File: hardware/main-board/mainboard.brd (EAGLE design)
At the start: 160 x 100 mm, 51 parts, among them J2 ADDRESS BUS, J3 DATA BUS, J5 IO_ADDRESS, J6 IO_DATA, J7 IO_CONTROLS, U1 AS6C1008-55PCN, U2 CD4001BE, U4 SST39SF010A-70-4C-NHEMICROCHI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

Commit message: closer to layout complete for z80Computer
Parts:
- added LED10, LED11, LED12, LED13, LED14, LED15, LED16, LED17, LED18, LED19, LED20, LED21, LED22, LED23, LED24, LED25, LED26, LED27, LED28, LED29, LED30, LED31, LED8, LED9: (no value), leds:LED-1206
- added LED32: Read Enable, leds:LED-1206
- added LED33: Output Enable, leds:LED-1206
- added R19, R20: 100 R, passives:0805
- moved R9 252.2 mm to (115.6, 8.89), turned to 180 degrees
- moved R8 234.0 mm to (111.8, 35.6), turned to 90 degrees
- moved J1 233.8 mm to (123.2, 3.81), turned to 180 degrees
- moved R10 229.4 mm to (115.6, 95.2), turned to 180 degrees
- moved LED2 226.3 mm to (120.7, 7.62)
- moved C6 224.6 mm to (120.7, 62.2), turned to 270 degrees
- moved R1 222.0 mm to (114.3, 14.0), turned to 180 degrees
- moved LED1 218.2 mm to (119.4, 12.7)
- moved C4 215.1 mm to (114.3, 35.6), turned to 90 degrees
- moved U2 213.7 mm to (118.1, 48.3)
- moved LED5 213.5 mm to (119.4, 16.5)
- moved S3 210.9 mm to (123.2, 87.6), turned to 180 degrees
- moved C7 208.0 mm to (90.2, 41.9), turned to 90 degrees
- moved LED4 207.2 mm to (119.4, 20.3)
- moved U$2 201.9 mm to (120.7, 39.4), turned to 180 degrees
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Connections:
- new net N$19: LED32.A, R19.1
- new net N$21: LED33.A, R20.1
- new net READ_ENABLE_LOW#: R19.2, U$5.12
- new net WRITE_ENABLE_LOW#: R20.2, U$5.10
- net A0: now also LED8.A
- net A1: now also LED9.A
- net A10: now also LED18.A
- net A11: now also LED19.A
- net A12: now also LED20.A
- net A13: now also LED21.A
- net A14: now also LED22.A
- net A15: now also LED23.A
- net A2: now also LED10.A
- net A3: now also LED11.A
- net A4: now also LED12.A
- net A5: now also LED13.A
- net A6: now also LED14.A
- net A7: now also LED15.A
- net A8: now also LED16.A
- net A9: now also LED17.A
- net D0: now also LED24.A
- net D1: now also LED25.A
- net D2: now also LED26.A
- net D3: now also LED27.A
- net D4: now also LED28.A
- net D5: now also LED29.A
- net D6: now also LED30.A
- net D7: now also LED31.A
- net GND: now also LED10.C, LED11.C, LED12.C, LED13.C, LED14.C, LED15.C, LED16.C, LED17.C, LED18.C, LED19.C, LED20.C, LED21.C, LED22.C, LED23.C, LED24.C, LED25.C, LED26.C, LED27.C, LED28.C, LED29.C, LED30.C, LED31.C, LED32.C, LED33.C, LED8.C, LED9.C
- net READ_ENABLE_LOW: now also U$5.13
- net WRITE_ENABLE_LOW: now also U$5.11
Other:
- board size 160 x 100 mm -> 127 x 100 mm

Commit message: main board starting to route
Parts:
- moved S1 83.4 mm to (98.3, 5.08), turned to 90 degrees
- moved LED2 57.5 mm to (63.8, 15.9), turned to 270 degrees
- moved LED1 56.8 mm to (63.8, 24.0), turned to 90 degrees
- moved U1 54.7 mm to (8.64, 59.3), turned to 180 degrees
- moved C5 54.6 mm to (89.4, 36.7), turned to 180 degrees
- moved C7 54.6 mm to (41.1, 17.9), turned to 180 degrees
- moved LED5 50.2 mm to (87.5, 55.2), turned to 90 degrees
- moved R9 49.6 mm to (66.7, 17.3), turned to 0 degrees
- moved R10 49.2 mm to (122.4, 46.5), turned to 0 degrees
- moved C6 48.5 mm to (72.8, 54.4), turned to 180 degrees
- moved R1 48.4 mm to (66.7, 22.6), turned to 0 degrees
- moved R17 46.5 mm to (77.3, 40.3)
- moved R18 46.5 mm to (77.3, 42.8)
- moved U2 45.4 mm to (74.7, 35.2)
- moved LED7 44.4 mm to (81.7, 42.8)
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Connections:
- removed net A14: J2.16, LED22.A
- removed net A15: J2.17, LED23.A
- removed net N$20: IC1.20
- net A14-SWITCH: now also J2.16, LED22.A
- net A15-SRAM-A14: now also J2.17, LED23.A
- net IORQ: now also IC1.20
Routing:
- net V5: track 0.00 -> 558.5 mm
- net A11: track 0.00 -> 92.6 mm
- net A12: track 0.00 -> 88.5 mm
- net A13: track 0.00 -> 87.3 mm
- net A10: track 0.00 -> 87.1 mm
- net A14-SWITCH: track 0.00 -> 85.1 mm
- net A9: track 0.00 -> 82.5 mm
- net A15-SRAM-A14: track 0.00 -> 82.3 mm
- net A8: track 0.00 -> 78.9 mm
- net A7: track 0.00 -> 75.5 mm
- net A6: track 0.00 -> 71.8 mm
- net A5: track 0.00 -> 69.1 mm
- net A4: track 0.00 -> 66.7 mm
- net A3: track 0.00 -> 64.1 mm
- net A2: track 0.00 -> 62.7 mm
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
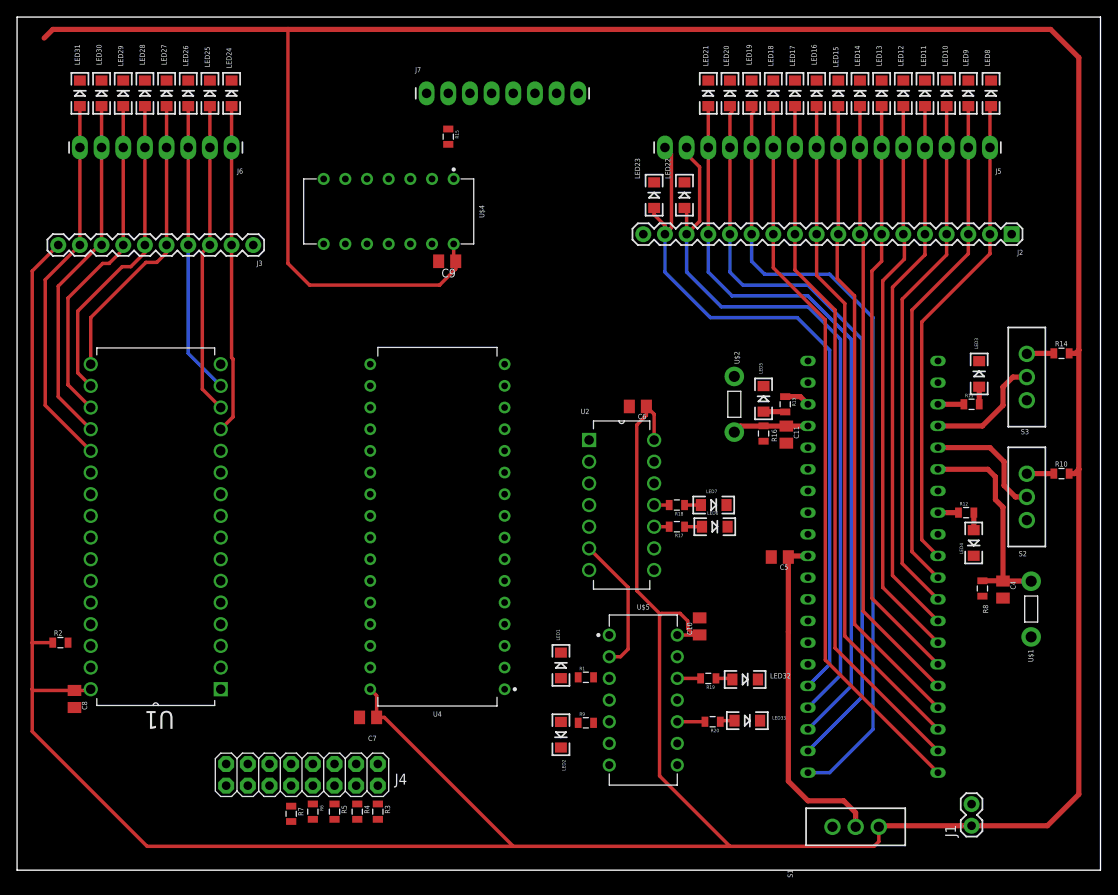
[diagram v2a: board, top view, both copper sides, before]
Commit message: update on clock board, so much cleaner now re-layout of main board
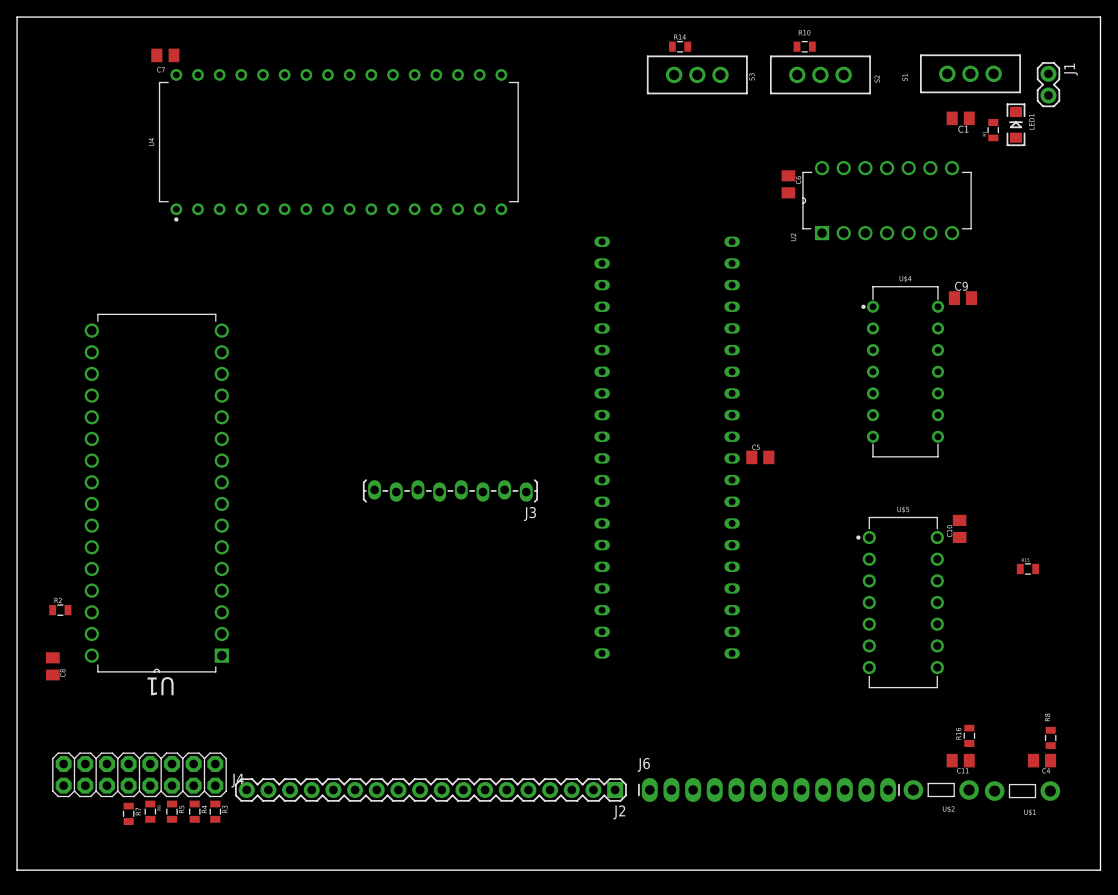
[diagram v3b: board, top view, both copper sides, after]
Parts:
- removed J5: IO_ADDRESS, connector:1X16_LONGPADS
- removed J7: IO_CONTROLS, connector:1X08_LONGPADS
- removed LED10, LED11, LED12, LED13, LED14, LED15, LED16, LED17, LED18, LED19, LED20, LED21, LED22, LED23, LED24, LED25, LED26, LED27, LED28, LED29, LED3, LED30, LED31, LED4, LED5, LED8, LED9: (no value), leds:LED-1206
- removed LED2: SRAM, leds:LED-1206
- removed LED32: Read Enable, leds:LED-1206
- removed LED33: Output Enable, leds:LED-1206
- removed LED6, LED7: OP Code Fetch, leds:LED-1206
- removed R11, R12, R13, R17, R18, R19, R20, R9: 100 R, passives:0805
- added C1: 10 uF, passives:C0805K
- J2: value ADDRESS BUS -> (none)
- J3: value DATA BUS -> (none); device connector:1X10 -> connector:1X08_LOCK_LONGPADS
- J6: value IO_DATA -> IO_CONTROLS; device connector:1X08_LONGPADS -> connector:1X12_LONGPADS
- LED1: value FLASH MEM -> (none)
- R1: value 100 R -> 1 K
- moved J6 89.9 mm to (74.2, 9.40), turned to 0 degrees
- moved S1 89.3 mm to (111.8, 93.3)
- moved J1 88.6 mm to (120.9, 93.3), turned to 270 degrees
- moved R15 84.8 mm to (118.5, 35.3), turned to 0 degrees
- moved LED1 82.8 mm to (117.1, 87.4)
- moved C7 81.1 mm to (17.4, 95.5)
- moved J2 80.0 mm to (70.1, 9.40)
- moved R1 80.0 mm to (114.4, 86.7), turned to 90 degrees
- moved U$4 63.4 mm to (104.1, 58.4), turned to 0 degrees
- moved C9 60.6 mm to (110.9, 67.1), turned to 0 degrees
- moved U2 58.6 mm to (109.6, 82.3), turned to 90 degrees
- moved R10 58.4 mm to (92.3, 96.5)
- moved R14 57.4 mm to (77.7, 96.5)
- moved S2 55.1 mm to (94.2, 93.2), turned to 270 degrees
- moved S3 52.4 mm to (79.7, 93.2), turned to 270 degrees
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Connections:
- removed net IRQ_ACK: R18.2, U2.11
- removed net N$10: LED3.A, R11.2
- removed net N$11: LED4.A, R12.2
- removed net N$12: IC1.28, R12.1
- removed net N$13: LED2.A, R9.1
- removed net N$14: IC1.18, R13.1
- removed net N$15: LED5.A, R13.2
- removed net N$17: LED6.A, R17.1
- removed net N$18: LED7.A, R18.1
- removed net N$19: LED32.A, R19.1
- removed net N$21: LED33.A, R20.1
- removed net N$3: C5.1, IC1.11, S1.2
- removed net OP_CODE_FETCH: R17.2, U2.10
- removed net READ_ENABLE_LOW#: R19.2, U$5.12
- removed net WRITE_ENABLE_LOW#: R20.2, U$5.10
- new net HALT: IC1.18, J6.11
- new net RFSH: IC1.28, J6.10
- new net VIN: J1.1, S1.3
- net A0: no longer J5.1, LED8.A
- net A1: no longer J5.2, LED9.A
- net A10: no longer J5.11, LED18.A
- net A11: no longer J5.12, LED19.A
- net A12: no longer J5.13, LED20.A
- net A13: no longer J5.14, LED21.A
- net A14-SWITCH: no longer J5.15, LED22.A
- net A15-SRAM-A14: no longer J5.16, LED23.A
- net A2: no longer J5.3, LED10.A
- net A3: no longer J5.4, LED11.A
- net A4: no longer J5.5, LED12.A
- net A5: no longer J5.6, LED13.A
- net A6: no longer J5.7, LED14.A
- net A7: no longer J5.8, LED15.A
- net A8: no longer J5.9, LED16.A
- net A9: no longer J5.10, LED17.A
- net BUSAK: now also J6.6; no longer J7.6, R11.1
- net BUSRQ: now also J6.7; no longer J7.7
- net D0: now also J3.1; no longer J3.2, J6.1, LED24.A
- net D1: now also J3.2; no longer J3.3, J6.2, LED25.A
- net D2: now also J3.3; no longer J3.4, J6.3, LED26.A
- net D3: now also J3.4; no longer J3.5, J6.4, LED27.A
- net D4: now also J3.5; no longer J3.6, J6.5, LED28.A
- net D5: now also J3.6; no longer J3.7, J6.6, LED29.A
- net D6: now also J3.7; no longer J3.8, J6.7, LED30.A
- net D7: now also J3.8; no longer J3.9, J6.8, LED31.A
- net FLASH_MEM_CS: no longer R1.2
- net GND: now also C1.2, J6.1; no longer J3.1, J7.1, LED10.C, LED11.C, LED12.C, LED13.C, LED14.C, LED15.C, LED16.C, LED17.C, LED18.C, LED19.C, LED2.C, LED20.C, LED21.C, LED22.C, LED23.C, LED24.C, LED25.C, LED26.C, LED27.C, LED28.C, LED29.C, LED3.C, LED30.C, LED31.C, LED32.C, LED33.C, LED4.C, LED5.C, LED6.C, LED7.C, LED8.C, LED9.C
- net INT: now also J6.2; no longer J7.2
- net IORQ: now also J6.8; no longer U2.13
- net M1: now also J6.9; no longer U2.12, U2.9
- net MREQ: no longer U2.8
- net READ_ENABLE_LOW: now also J6.4; no longer J7.4, U$5.13
- net SRAM_CS: no longer R9.2
- net SYS_CLK: now also J6.5; no longer J7.5
- net V5: now also C1.1, C5.1, IC1.11, J6.12, R1.2, S1.2; no longer J1.1, J3.10, J7.8, S1.3
- net WAIT: now also J6.3; no longer J7.3
- net WRITE_ENABLE_LOW: no longer U$5.11
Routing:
- net V5: track 558.5 -> 0.00 mm
- net A11: track 92.6 -> 0.00 mm
- net A12: track 88.5 -> 0.00 mm
- net A13: track 87.3 -> 0.00 mm
- net A10: track 87.1 -> 0.00 mm
- net A14-SWITCH: track 85.1 -> 0.00 mm
- net A9: track 82.5 -> 0.00 mm
- net A15-SRAM-A14: track 82.3 -> 0.00 mm
- net A8: track 78.9 -> 0.00 mm
- net A7: track 75.5 -> 0.00 mm
- net A6: track 71.8 -> 0.00 mm
- net A5: track 69.1 -> 0.00 mm
- net A4: track 66.7 -> 0.00 mm
- net A3: track 64.1 -> 0.00 mm
- net A2: track 62.7 -> 0.00 mm
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
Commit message: some routing complete
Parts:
- moved C6 33.5 mm to (123.2, 73.7), flipped to the bottom, turned to 90 degrees
- moved J3 23.7 mm to (50.7, 66.4)
- moved U2 11.3 mm to (103.8, 72.6), turned to 270 degrees
- moved C1 8.90 mm to (110.1, 97.0), flipped to the bottom, turned to 0 degrees
- moved R15 8.02 mm to (120.0, 43.2), flipped to the bottom, turned to 180 degrees
- moved C8 2.16 mm to (6.35, 23.9), flipped to the bottom
- moved C10 0.40 mm to (110.6, 40.4), flipped to the bottom
- moved R10 0.40 mm to (92.2, 96.9), flipped to the bottom, turned to 180 degrees
- moved C4 0.38 mm to (120.1, 12.4), flipped to the bottom, turned to 0 degrees
- moved R14 0.28 mm to (78.0, 96.6), flipped to the bottom, turned to 180 degrees
- moved R2 0.25 mm to (5.08, 30.2), flipped to the bottom, turned to 180 degrees
- moved R7 0.25 mm to (13.1, 6.86), flipped to the bottom
- moved C9 0.18 mm to (110.7, 67.2), flipped to the bottom, turned to 90 degrees
- moved C5 0.18 mm to (87.2, 48.3), flipped to the bottom, turned to 180 degrees
- moved C11 0.13 mm to (110.6, 12.7), flipped to the bottom, turned to 0 degrees
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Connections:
- net BUSAK: now also J6.4; no longer J6.6
- net IORQ: now also J6.10; no longer J6.8
- net M1: now also J6.8; no longer J6.9
- net READ_ENABLE_LOW: now also J6.3; no longer J6.4
- net RFSH: now also J6.9; no longer J6.10
- net SRAM-A15: now also J4.9; no longer J4.7
- net SRAM-A16: now also J4.7; no longer J4.9
- net WAIT: now also J6.6; no longer J6.3
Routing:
- net V5: track 0.00 -> 595.4 mm
- net A14-SWITCH: track 0.00 -> 126.2 mm
- net A12: track 0.00 -> 118.2 mm
- net A13: track 0.00 -> 107.9 mm
- net A11: track 0.00 -> 93.9 mm
- net A10: track 0.00 -> 75.2 mm
- net A9: track 0.00 -> 71.6 mm
- net A8: track 0.00 -> 68.0 mm
- net A7: track 0.00 -> 64.4 mm
- net A6: track 0.00 -> 60.8 mm
- net A5: track 0.00 -> 58.0 mm
- net RFSH: track 0.00 -> 54.2 mm
- net A4: track 0.00 -> 53.7 mm
- net A3: track 0.00 -> 50.1 mm
- net M1: track 0.00 -> 49.9 mm
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
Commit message: not sure
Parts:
- added U$3: CMD_C0DE_LOGOCMD_CODE_LOGO_SILK, logos:CMD_C0DE_LOGO_SILK
- J2: value (none) -> IO_ADDRESS
- J3: value (none) -> IO_DATA
- LED1: value (none) -> pwr
- S1: value (none) -> MAIN PWR
- moved R15 52.5 mm to (68.1, 35.6), turned to 0 degrees
- moved C5 20.2 mm to (67.1, 48.3), turned to 0 degrees
- moved IC1 2.54 mm to (78.7, 49.5), flipped to the top
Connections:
- net GND: now also J2.18; no longer J2.1
- net V5: now also J2.1; no longer J2.18
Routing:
- net WRITE_ENABLE_LOW: track 0.00 -> 186.4 mm, vias 0 -> 3
- net READ_ENABLE_LOW: track 21.6 -> 171.5 mm, vias 0 -> 3
- net D7: track 0.00 -> 146.5 mm, vias 0 -> 2
- net A7: track 64.4 -> 195.9 mm, vias 0 -> 3
- net A9: track 71.6 -> 198.2 mm, vias 0 -> 3
- net A8: track 68.0 -> 189.4 mm, vias 0 -> 2
- net D6: track 0.00 -> 119.2 mm, vias 0 -> 2
- net D4: track 0.00 -> 118.8 mm, vias 0 -> 3
- net D5: track 0.00 -> 116.9 mm, vias 0 -> 3
- net A4: track 53.7 -> 168.6 mm, vias 0 -> 4
- net A2: track 46.5 -> 160.7 mm, vias 0 -> 3
- net A10: track 75.2 -> 187.0 mm, vias 0 -> 2
- net A0: track 42.4 -> 154.2 mm, vias 0 -> 4
- net A3: track 50.1 -> 159.2 mm, vias 0 -> 3
- net A1: track 44.4 -> 153.2 mm, vias 0 -> 4
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- added copper zone on layer 1, net GND
- added copper zone on layer 16, net GND
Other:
- board text added: "A14-SWITCH"
- board text added: "A15-SRAM"
- board text added: "IORQ"
- board text added: "NMI"
- board text added: "RESET"
- board text added: "a0"
- board text added: "a1"
- board text added: "a10"
- board text added: "a11"
- board text added: "a12"
- board text added: "a13"
- board text added: "a2"
- board text added: "a3"
- board text added: "a4"
- board text added: "a5"
- board text added: "a6"
- board text added: "a7"
- board text added: "a8"
- board text added: "a9"
- board text added: "busak"
- board text added: "busrq"
- board text added: "d0"
- board text added: "d1"
- board text added: "d2"
- board text added: "d3"
- board text added: "d4"
- board text added: "d5"
- board text added: "d6"
- board text added: "d7"
- board text added: "gnd"
- board text added: "halt"
- board text added: "int"
- board text added: "m1"
- board text added: "read"
- board text added: "rfsh"
- board text added: "sys_clk"
- board text added: "v5"
- board text added: "wait"
- board text added: "z80"
